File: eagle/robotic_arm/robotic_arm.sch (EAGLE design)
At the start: 39 parts

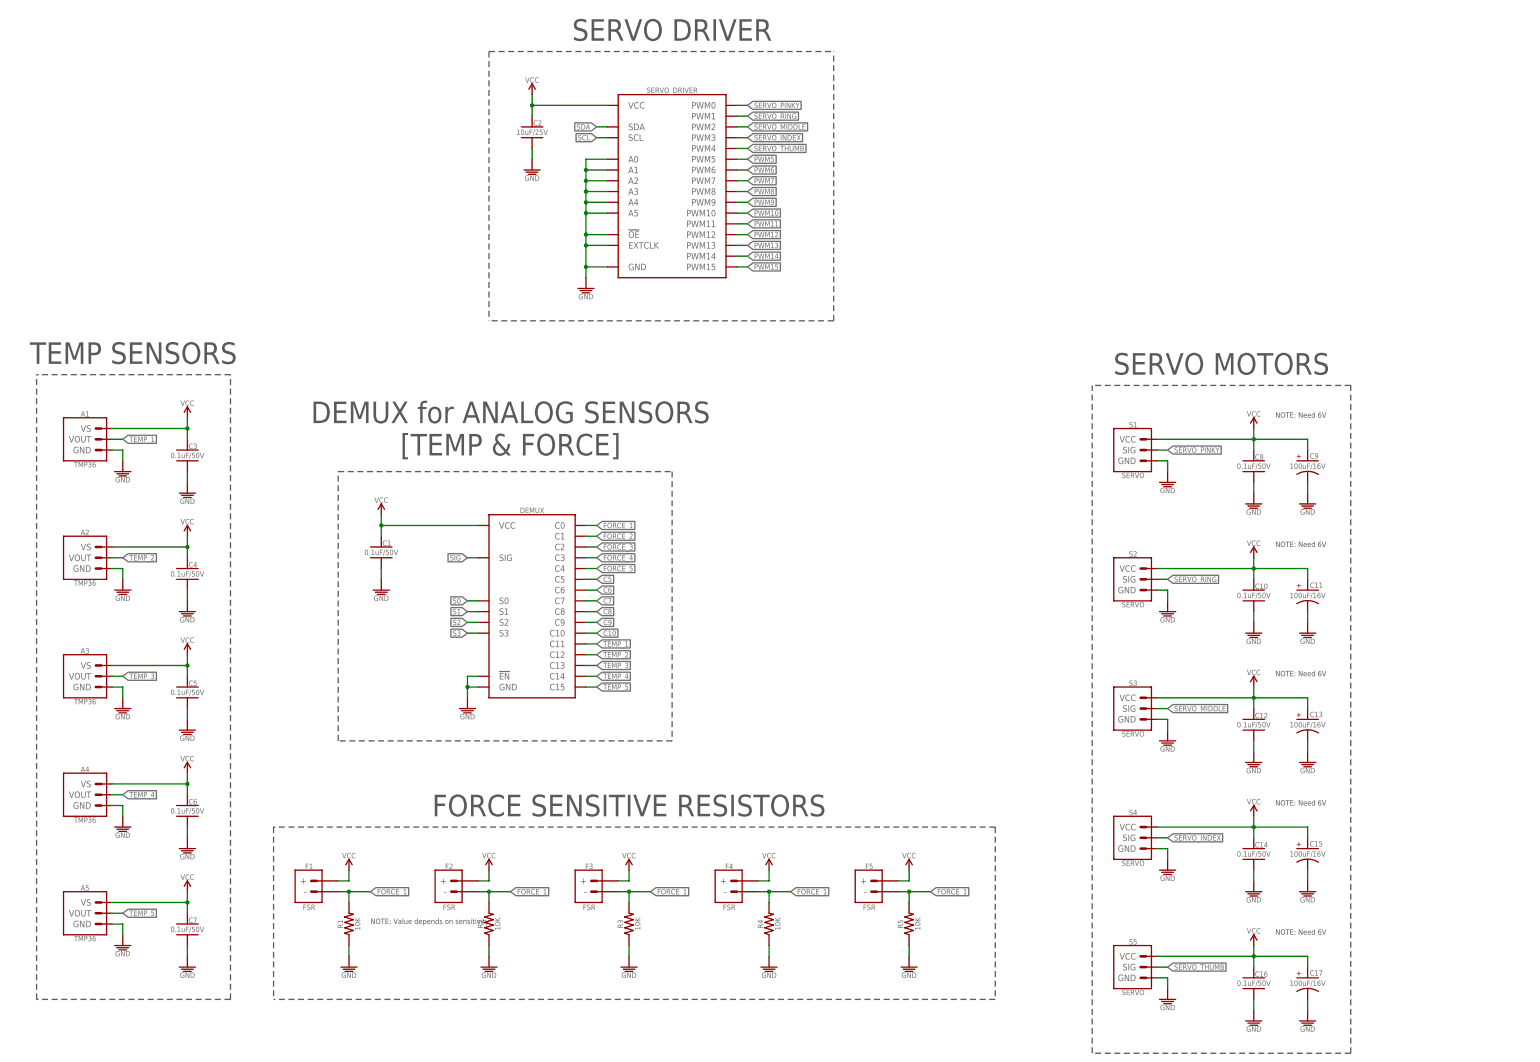
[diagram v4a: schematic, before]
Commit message: Modfied git ignore.  Added h bridge files.  Modified EAGLE files
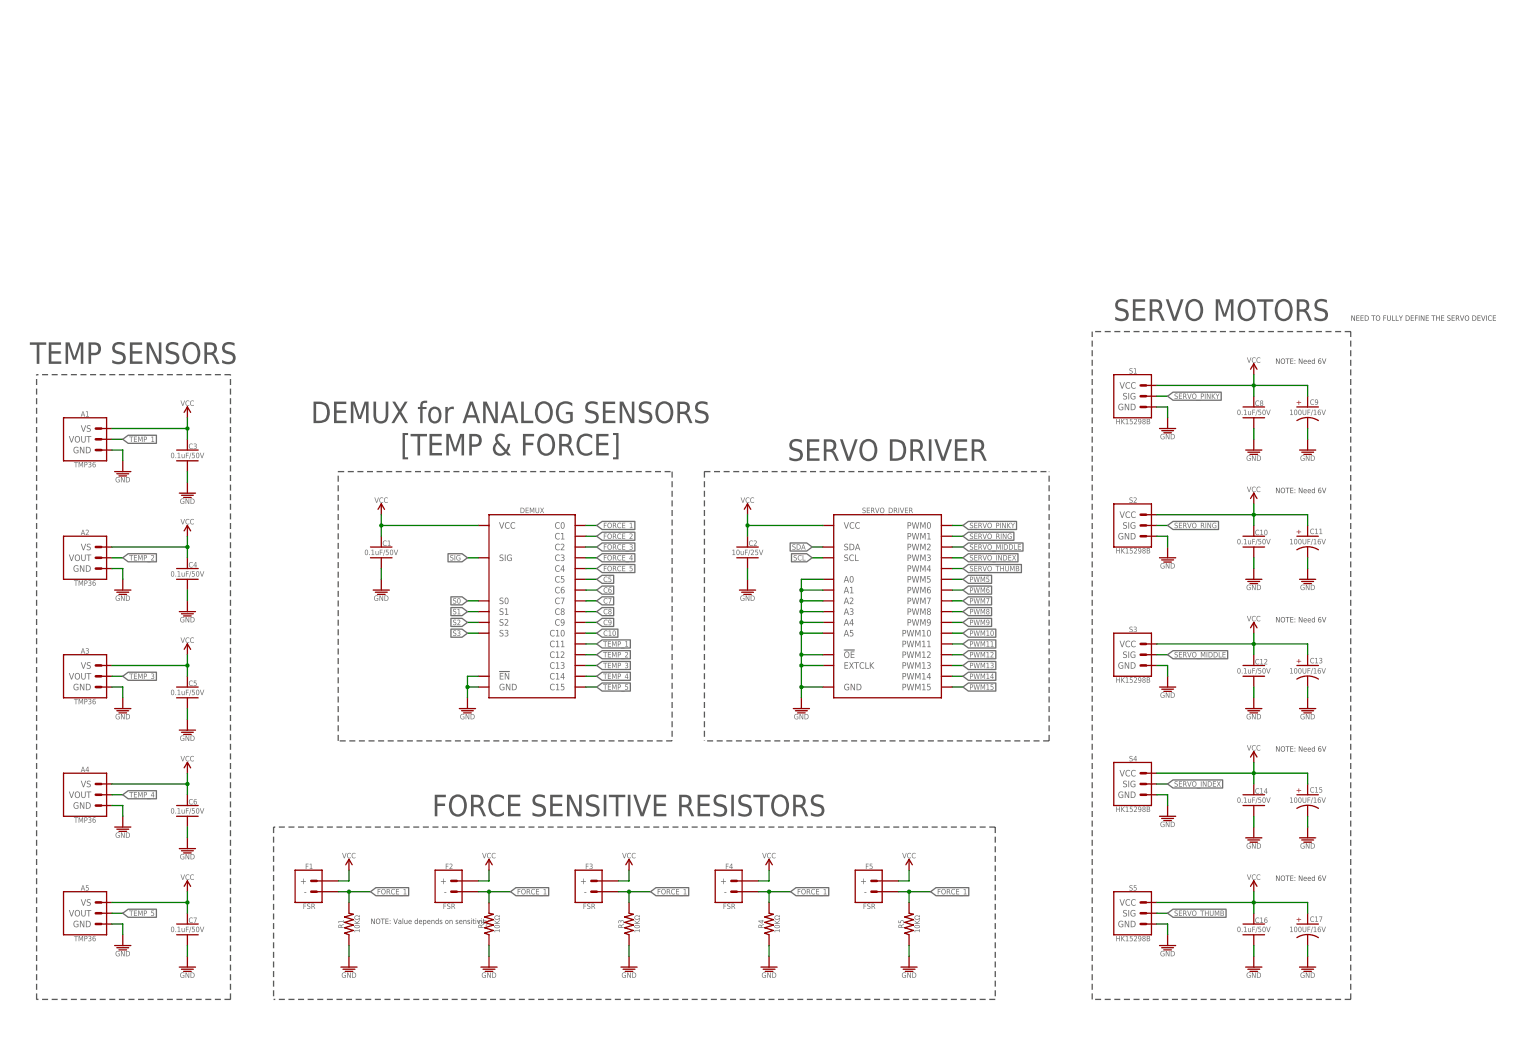
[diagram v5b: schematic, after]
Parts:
- A1, A2, A3, A4, A5: device MrSwirlyEyes:TMP36 -> MrSwirlyEyes:TEMPERATURE-SENSOR_TMP36
- C1, C10, C12, C14, C16, C3, C4, C5, C6, C7, C8: value CAP_CER_SMD-805_0.1UF-50V-10% -> 0.1uF/50V; device MrSwirlyEyes:CAP_CER_SMD-805_0.1UF-50V-10% -> MrSwirlyEyes:CAPACITOR_CERAMIC_SMD-805_0.1UF-50V-10%
- C11, C13, C15, C17, C9: value CAP_POL_ALUM-ELECTROLYTIC_SMD_100UF-16V-20% -> 100UF/16V; device MrSwirlyEyes:CAP_POL_ALUM-ELECTROLYTIC_SMD_100UF-16V-20% -> MrSwirlyEyes:CAPACITOR_POLARIZED_ALUM-ELECTROLYTIC_SMD_100UF-16V-20%
- C2: value CAP_CER_SMD-805_10UF-25V-10% -> 10uF/25V; device MrSwirlyEyes:CAP_CER_SMD-805_10UF-25V-10% -> MrSwirlyEyes:CAPACITOR_CERAMIC_SMD-805_10UF-25V-10%
- DEMUX: value CD74HC4067-SM96_16:1_MUX-DEMUX -> CH16_MUX-DEMUX
- F1, F2, F3, F4, F5: device MrSwirlyEyes:FSR -> MrSwirlyEyes:FSR_FORCE-SENSATIVE-RESISTOR_PRESS-SENSOR
- R1, R2, R3, R4, R5: value RES_SMD-805_10K-5%-1/8W -> 10KΩ; device MrSwirlyEyes:RES_SMD-805_10K-5%-1/8W -> MrSwirlyEyes:RESISTORSMD-0805_1/8W_10K_5%
- S1, S2, S3, S4, S5: value SERVO -> HK15298B; device MrSwirlyEyes:SERVO -> MrSwirlyEyes:SERVO-HK15298B
- SERVO_DRIVER: value PCA9685_16-CH_12-BIT_PWM-DRIVER -> PCA9685
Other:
- note added: "NEED TO FULLY DEFINE THE SERVO DEVICE"
- moved on the sheet: SERVO_DRIVER

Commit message: Rev 1 of Robotic Arm schematic complete
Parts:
- removed A1, A2, A3, A4, A5: TMP36, MrSwirlyEyes:TEMPERATURE-SENSOR_TMP36
- removed DEMUX: CH16_MUX-DEMUX, MrSwirlyEyes:CD74HC4067-SM96_16:1_MUX-DEMUX
- removed F1, F2, F3, F4, F5: FSR, MrSwirlyEyes:FSR_FORCE-SENSATIVE-RESISTOR_PRESS-SENSOR
- removed R1, R2, R3, R4, R5: 10KΩ, MrSwirlyEyes:RESISTORSMD-0805_1/8W_10K_5%
- removed SERVO_DRIVER: PCA9685, MrSwirlyEyes:PCA9685_16-CH_12-BIT_PWM-DRIVER
- added A6: ANTENNASMD5, lib_kenmei:ANTENNASMD5
- added B1: 748421245, lib_kenmei:BALUN0805
- added BATT1: BATTERYPTH_HOLES, MrSwirlyEyes:BATTERYPTH_HOLES
- added C18, C25, C82, C92, C94, C95, C97: 10uF/25V, MrSwirlyEyes:CAP_CERAMIC_SMD-805_10UF-25V-10%
- added C19, C26, C47, C48, C49, C50, C51, C52, C54, C56, C63, C79, C81, C83, C93, C96, C98: 0.1uF/50V, MrSwirlyEyes:CAP_CERAMIC_SMD-805_0.1UF-50V-10%
- added C20: 1000uF/50V, MrSwirlyEyes:CAP_POLARIZED_ALUM-ELECTROLYTIC_PTH_1000UF-50V-20%
- added C53, C55, C57, C58, C64, C85: 1uF/25V, MrSwirlyEyes:CAP_CERAMIC_SMD-805-1UF-25V-10%
- added C59, C60: 12pF/250V, MrSwirlyEyes:CAP_CERAMIC_SMD-805_12PF-250V-5%
- added C61: 22PF/250V, MrSwirlyEyes:CAP_CERAMIC_SMD-805_22PF-250V-5%
- added C62: 0.75PF/100V, MrSwirlyEyes:CAP_CERAMIC_SMD-805-0.75PF-100V-33%
- added C80: 220uF/16V, MrSwirlyEyes:CAP_POLARIZED_ALUM-ELECTROLYTIC_SMD_220UF-16V-20%
- added C84: 100UF/16V, MrSwirlyEyes:CAP_POLARIZED_ALUM-ELECTROLYTIC_SMD_100UF-16V-20%
- added D6, D7: 1A/50V, MrSwirlyEyes:DIODE_GEN-PURPSMD_GP_1A-50V-SOD123F
- added DEMUX1: CH16_MUX-DEMUX, MrSwirlyEyes:CD74HC4067-SM96_16:1_MUX-DEMUX
- added FSR1, FSR2, FSR3, FSR4, FSR5: FSR, MrSwirlyEyes:FSR_FORCE-SENSATIVE-RESISTOR_PRESS-SENSOR
- added J1: (no value), MrSwirlyEyes:AVR_SPI_PRG_6NS
- added J2: (ID,OD)=(2.1,5.5)MM, MrSwirlyEyes:POWER_JACK-BARREL_ID2.1MM-OD5.5MM
- added JP1: FTDIPTH-RA, MrSwirlyEyes:FTDIPTH-RA
- added L1, L2: 10uH, MrSwirlyEyes:INDUCTORSMD-805_10UH-0.5A-0.65OHM-10%
- added PWM_DRIVER: PCA9685, MrSwirlyEyes:PCA9685_16-CH_12-BIT_PWM-DRIVER
- added R16, R39, R40, R41, R42, R43: 10KΩ, MrSwirlyEyes:RESISTORSMD-0805_1/8W_10K_5%
- added R17, R18: 4.7K, MrSwirlyEyes:RESISTORSMD-0805_1/8W_4.7K_5%
- added S6: HK15298B, MrSwirlyEyes:SERVO-HK15298B
- added SW1: 5A/28V, MrSwirlyEyes:SWITCH_SPDT5A-28V_13L-7W
- added TEMP1, TEMP2, TEMP3, TEMP4, TEMP5: TMP36, MrSwirlyEyes:TEMPERATURE-SENSOR_TMP36
- added U$1, U$2: NET_BRIDGE, MrSwirlyEyes:NET_BRIDGE
- added U6: ATMEGA128RFA1, MrSwirlyEyes:ATMEGA128RFA1
- added VREG1: 5A/5V, MrSwirlyEyes:VREG_MIC29501-5.0_LINEAR_ULDO_5A-5VMIC29501-5.0_5A-5V
- added VREG3: 1A/3.3V, MrSwirlyEyes:VREG_TPS76833_ULDO_FAST-TRANSIENT_1A-3.3VTPS76833QDR_1A-3.3V
- added Y1: 16MHz, MrSwirlyEyes:CRYSTAL_ABM3B_16MHZ_18PF
- C1, C10, C12, C14, C16, C3, C4, C5, C6, C7, C8: device MrSwirlyEyes:CAPACITOR_CERAMIC_SMD-805_0.1UF-50V-10% -> MrSwirlyEyes:CAP_CERAMIC_SMD-805_0.1UF-50V-10%
- C11, C13, C15, C17, C9: device MrSwirlyEyes:CAPACITOR_POLARIZED_ALUM-ELECTROLYTIC_SMD_100UF-16V-20% -> MrSwirlyEyes:CAP_POLARIZED_ALUM-ELECTROLYTIC_SMD_100UF-16V-20%
- C2: value 10uF/25V -> 100UF/16V; device MrSwirlyEyes:CAPACITOR_CERAMIC_SMD-805_10UF-25V-10% -> MrSwirlyEyes:CAP_POLARIZED_ALUM-ELECTROLYTIC_SMD_100UF-16V-20%
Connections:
- removed net FORCE_1: DEMUX.C0, F1.-, F2.-, F3.-, F4.-, F5.-, R1.2, R2.2, R3.2, R4.2, R5.2
- removed net FORCE_2: DEMUX.C1
- removed net FORCE_3: DEMUX.C2
- removed net FORCE_4: DEMUX.C3
- removed net FORCE_5: DEMUX.C4
- removed net PWM5: SERVO_DRIVER.PWM5
- removed net TEMP_1: A1.VOUT, DEMUX.C11
- removed net TEMP_2: A2.VOUT, DEMUX.C12
- removed net TEMP_3: A3.VOUT, DEMUX.C13
- removed net TEMP_4: A4.VOUT, DEMUX.C14
- removed net TEMP_5: A5.VOUT, DEMUX.C15
- new net 3.3V: C83.1, C94.1, D7.A, VREG1.VOUT
- new net 5V: C1.1, C10.1, C11.A, C12.1, C13.A, C14.1, C15.A, C16.1, C17.A, C2.A, C8.1, C9.A, S1.VCC, S2.VCC, S3.VCC, S4.VCC, S5.VCC, S6.VCC
- new net A0: U6.PF0(ADC0)
- new net A1: U6.PF1(ADC1)
- new net A2: U6.PF2(ADC2/DIG2)
- new net A3: U6.PF3(ADC3/DIG4)
- new net A4: U6.PF4(ADC4/TCK)
- new net A5: U6.PF5(ADC5/TMS)
- new net A6: U6.PF6(ADC6/TDO)
- new net A7: U6.PF7(ADC7/TDI)
- new net FSR_INDEX: DEMUX1.C3, FSR4.-, R41.2
- new net FSR_MIDDLE: DEMUX1.C2, FSR3.-, R40.2
- new net FSR_PINKY: DEMUX1.C0, FSR1.-, R16.2
- new net FSR_RING: DEMUX1.C1, FSR2.-, R39.2
- new net FSR_THUMB: DEMUX1.C4, FSR5.-, R42.2
- new net MISO: J1.1, U6.PB3(MISO/PDO/PCINT3)
- new net MOSI: J1.4, U6.PB2(MOSI/PDI/PCINT2)
- new net N$1: C20.A, C80.A, C81.1, C82.1, C84.A, C95.1, C96.1, C97.1, C98.1, D6.K, D7.K, SW1.S1, VREG1.EN, VREG1.VIN, VREG3.VIN
- new net N$2: BATT1.N, J2.GND@1
- new net N$30: C60.1, U6.XTAL1, Y1.2
- new net N$32: B1.OUT2, U6.RFN
- new net N$33: B1.OUT1, U6.RFP
- new net N$34: B1.GND@2, C61.1
- new net N$35: C59.1, U6.XTAL2, Y1.1
- new net N$38: L2.2, U$2.P$1
- new net N$39: A6.SIGNAL, B1.IN, C62.1
- new net N$41: C79.1, JP1.2
- new net N$42: JP1.5
- new net N$43: BATT1.P, J2.PWR, SW1.P
- new net NGND: C85.2, U$1.P$1, U$2.P$2
- new net PB4: U6.PB4(OC2A/PCINT4)
- new net PB5: U6.PB5(OC1A/PCINT5)
- new net PB6: U6.PB6(OC1B/PCINT6)
- new net PB7: U6.PB7(OC0A/OC1C/PCINT7)
- new net PD4: U6.PD4(ICP1)
- new net PD5: U6.PD5(XCK1)
- new net PD6: U6.PD6(T1)
- new net PD7: U6.PD7(T0)
- new net PE2: U6.PE2(XCK0/AIN0)
- new net PE3: U6.PE3(OC3A/AIN1)
- new net PE4: U6.PE4(OC3B/INT4)
- new net PE5: U6.PE5(OC3C/INT5)
- new net PE6: U6.PE6(T3/INT6)
- new net PE7: U6.PE7(ICP3/INT7/CLKO)
- new net PG0: U6.PG0(DIG3)
- new net PG1: U6.PG1(DIG1)
- new net PG2: U6.PG2(AMR)
- new net PG3: U6.PG3(TOSC2)
- new net PG4: U6.PG4(TOSC1)
- new net PG5: U6.PG5(OC0B)
- new net RESET: C79.2, J1.5, R43.1, U6.RSTN
- new net RX0: JP1.4, U6.PE0(RXD0/PCINT8)
- new net RX1: U6.PD2(RXD1/INT2)
- new net SCK: J1.3, U6.PB1(SCK/PCINT1)
- new net SERVO_WRIST: PWM_DRIVER.PWM5, S6.SIG
- new net SSN: U6.PB0(SSN/PCINT0)
- new net TEMP_INDEX: DEMUX1.C14, TEMP4.VOUT
- new net TEMP_MIDDLE: DEMUX1.C13, TEMP3.VOUT
- new net TEMP_PINKY: DEMUX1.C11, TEMP1.VOUT
- new net TEMP_RING: DEMUX1.C12, TEMP2.VOUT
- new net TEMP_THUMB: DEMUX1.C15, TEMP5.VOUT
- new net TX0: JP1.3, U6.PE1(TXD0)
- new net TX1: U6.PD3(TXD1/INT3)
- net C10: now also DEMUX1.C10; no longer DEMUX.C10
- net C5: now also DEMUX1.C5; no longer DEMUX.C5
- net C6: now also DEMUX1.C6; no longer DEMUX.C6
- net C7: now also DEMUX1.C7; no longer DEMUX.C7
- net C8: now also DEMUX1.C8; no longer DEMUX.C8
- net C9: now also DEMUX1.C9; no longer DEMUX.C9
- net GND: now also B1.GND@5, C18.2, C19.2, C2.K, C20.K, C25.2, C26.2, C47.2, C48.2, C49.2, C50.2, C51.2, C52.2, C53.2, C54.2, C55.2, C56.2, C57.2, C58.2, C59.2, C60.2, C61.2, C62.2, C63.2, C64.2, C80.K, C81.2, C82.2, C83.2, C84.K, C92.2, C93.2, C94.2, C95.2, C96.2, C97.2, C98.2, DEMUX1.!EN, DEMUX1.GND, J1.6, J2.GND@2, JP1.6, L2.1, PWM_DRIVER.!OE, PWM_DRIVER.A0, PWM_DRIVER.A1, PWM_DRIVER.A2, PWM_DRIVER.A3, PWM_DRIVER.A4, PWM_DRIVER.A5, PWM_DRIVER.EXTCLK, PWM_DRIVER.GND, R16.1, R39.1, R40.1, R41.1, R42.1, S6.GND, TEMP1.GND, TEMP2.GND, TEMP3.GND, TEMP4.GND, TEMP5.GND, U$1.P$2, U6.AVSS, U6.AVSS_RFN, U6.AVSS_RFP, U6.CLKI, U6.DVSS, U6.TST, VREG1.GND, VREG3.!EN, VREG3.GND; no longer A1.GND, A2.GND, A3.GND, A4.GND, A5.GND, C2.2, DEMUX.!EN, DEMUX.GND, R1.1, R2.1, R3.1, R4.1, R5.1, SERVO_DRIVER.!OE, SERVO_DRIVER.A0, SERVO_DRIVER.A1, SERVO_DRIVER.A2, SERVO_DRIVER.A3, SERVO_DRIVER.A4, SERVO_DRIVER.A5, SERVO_DRIVER.EXTCLK, SERVO_DRIVER.GND
- net PWM10: now also PWM_DRIVER.PWM10; no longer SERVO_DRIVER.PWM10
- net PWM11: now also PWM_DRIVER.PWM11; no longer SERVO_DRIVER.PWM11
- net PWM12: now also PWM_DRIVER.PWM12; no longer SERVO_DRIVER.PWM12
- net PWM13: now also PWM_DRIVER.PWM13; no longer SERVO_DRIVER.PWM13
- net PWM14: now also PWM_DRIVER.PWM14; no longer SERVO_DRIVER.PWM14
- net PWM15: now also PWM_DRIVER.PWM15; no longer SERVO_DRIVER.PWM15
- net PWM6: now also PWM_DRIVER.PWM6; no longer SERVO_DRIVER.PWM6
- net PWM7: now also PWM_DRIVER.PWM7; no longer SERVO_DRIVER.PWM7
- net PWM8: now also PWM_DRIVER.PWM8; no longer SERVO_DRIVER.PWM8
- net PWM9: now also PWM_DRIVER.PWM9; no longer SERVO_DRIVER.PWM9
- net S0: now also DEMUX1.S0; no longer DEMUX.S0
- net S1: now also DEMUX1.S1; no longer DEMUX.S1
- net S2: now also DEMUX1.S2; no longer DEMUX.S2
- net S3: now also DEMUX1.S3; no longer DEMUX.S3
- net SCL: now also PWM_DRIVER.SCL, R17.1, U6.PD0(SCL/INT0); no longer SERVO_DRIVER.SCL
- net SDA: now also PWM_DRIVER.SDA, R18.1, U6.PD1(SDA/INT1); no longer SERVO_DRIVER.SDA
- net SERVO_INDEX: now also PWM_DRIVER.PWM3; no longer SERVO_DRIVER.PWM3
- net SERVO_MIDDLE: now also PWM_DRIVER.PWM2; no longer SERVO_DRIVER.PWM2
- net SERVO_PINKY: now also PWM_DRIVER.PWM0; no longer SERVO_DRIVER.PWM0
- net SERVO_RING: now also PWM_DRIVER.PWM1; no longer SERVO_DRIVER.PWM1
- net SERVO_THUMB: now also PWM_DRIVER.PWM4; no longer SERVO_DRIVER.PWM4
- net SIG: now also DEMUX1.SIG; no longer DEMUX.SIG
- net VCC: now also C18.1, C19.1, C25.1, C26.1, C47.1, C48.1, C49.1, C50.1, C51.1, C52.1, C53.1, C54.1, C55.1, C56.1, C57.1, C58.1, C63.1, C64.1, C85.1, C92.1, C93.1, D6.A, DEMUX1.VCC, FSR1.+, FSR2.+, FSR3.+, FSR4.+, FSR5.+, J1.2, JP1.1, L1.1, L1.2, PWM_DRIVER.VCC, R17.2, R18.2, R43.2, TEMP1.VS, TEMP2.VS, TEMP3.VS, TEMP4.VS, TEMP5.VS, U6.AREF, U6.AVDD, U6.DEVDD, U6.DVDD, U6.EVDD, VREG3.VOUT; no longer A1.VS, A2.VS, A3.VS, A4.VS, A5.VS, C1.1, C10.1, C11.A, C12.1, C13.A, C14.1, C15.A, C16.1, C17.A, C2.1, C8.1, C9.A, DEMUX.VCC, F1.+, F2.+, F3.+, F4.+, F5.+, S1.VCC, S2.VCC, S3.VCC, S4.VCC, S5.VCC, SERVO_DRIVER.VCC
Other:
- note added: "47K?"
- note added: "ACTUATORS"
- note added: "ATMEGA128RFA1"
- note added: "AVR ISP"
- note added: "CHECK THESE FOR ACCURACY"
- note added: "DEMULTIPLEXER"
- note added: "FTDI"
- note added: "I2C ADDR: x40"
- note added: "LPF"
- note added: "MCU"
- note added: "Might add op amps"
- note added: "NC"
- note added: "POWER SYSTEM"
- note added: "PROGRAMMER"
- note added: "PWM DRIVER [TEC + VIBE]"
- note added: "SENSORS"
- note added: "SERVOS"
- note removed: "DEMUX for ANALOG SENSORS [TEMP & FORCE]"
- note removed: "NOTE: Need 6V"
- note removed: "SERVO DRIVER"
- moved on the sheet: C1, C10, C11, C12, C13, C14, C15, C16, C17, C3, C4, C5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

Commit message: Rev 1:  Robotic Arm.  Tidied up schematic
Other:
- note added: "ANALOG DEMUX"
- note added: "PWM DRIVER"
- note removed: "DEMULTIPLEXER"
- note removed: "PWM DRIVER [TEC + VIBE]"
- note removed: "SERVO MOTORS"
- moved on the sheet: A6, B1, BATT1, C1, C10, C11, C12, C13, C14, C15, C16, C17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

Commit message: Rev 1:  Robotic Arm.  Added reset button to MCU.  Modified several of the component symbols.  Resized board
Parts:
- added D1: 1A/50V, MrSwirlyEyes:DIODE_GEN-PURPSMD_GP_1A-50V-SOD123F
- added S7: TACTILE-SW_500mA/12V, MrSwirlyEyes:SWITCH_MOMENTARY_SPSTSPST-SMD-50MA-12V_L5.2-W5.2
- AVR_ISP: value (none) -> AVR ISP
- renumbered J1 to AVR_ISP
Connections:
- net GND: now also S7.1
- net RESET: now also D1.A, S7.2
- net VCC: now also D1.K
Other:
- note added: "ROBOTIC ARM"
- note added: "Rev 1"
- note added: "TRANSMISSION OF TOUCH VR"
- note added: "add diode CD1206-S01575"
- moved on the sheet: C18, C19, C25, C26, C79, DEMUX1, JP1, PWM_DRIVER, R43
